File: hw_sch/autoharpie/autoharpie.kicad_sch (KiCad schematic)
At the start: 0 parts

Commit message: DAC, touch sensors
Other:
- added sheet Audio Interface (audio.kicad_sch)
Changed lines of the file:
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@@
+    )
+  )
+  (sheet (at 208.28 72.39) (size 62.23 34.29) (fields_autoplaced)
+    (stroke (width 0.1524) (type solid))
+    (fill (color 0 0 0 0.0000))
+    (property "Sheetname" "Audio Interface" (at 208.28 71.6784 0)
+      (effects (font (size 1.27 1.27)) (justify left bottom))
+    )
+    (property "Sheetfile" "audio.kicad_sch" (at 208.28 107.2646 0)
+      (effects (font (size 1.27 1.27)) (justify left top))
+    )
+    (instances
+      (project "autoharpie"
+        (path "/f22a88c4-866b-40a0-9fc2-96344be0ec71" (page "30"))
+      )
     )
   )

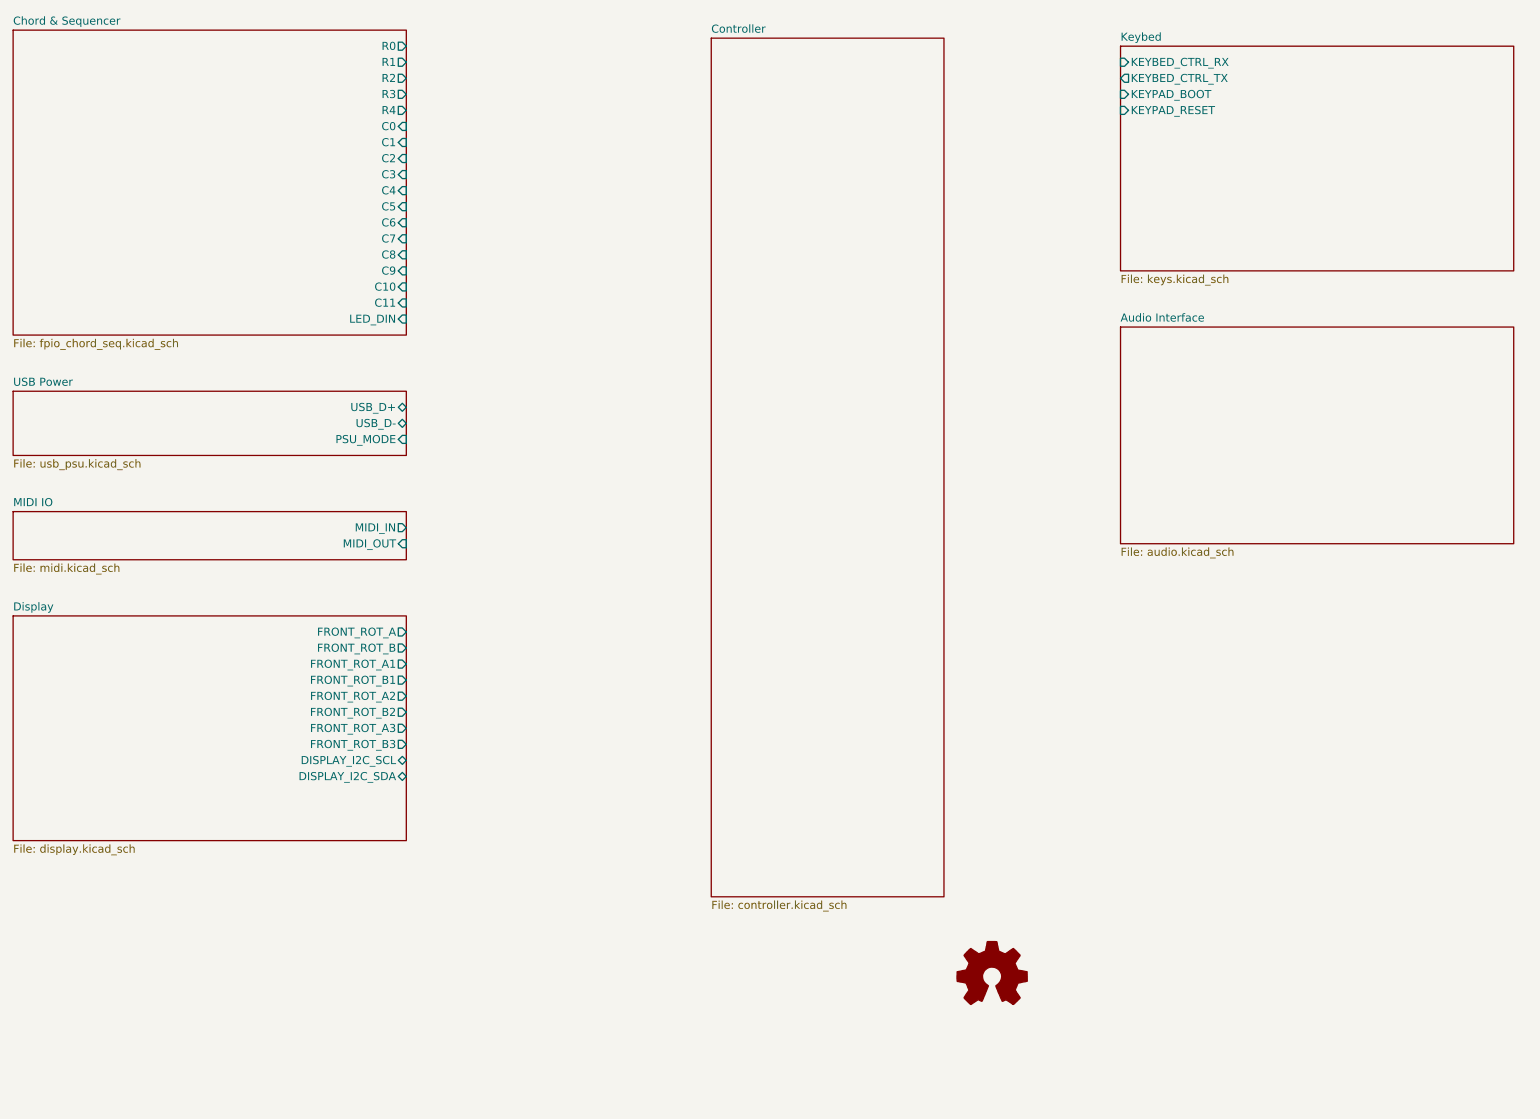
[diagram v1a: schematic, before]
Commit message: DAC wiring, add heirch pins
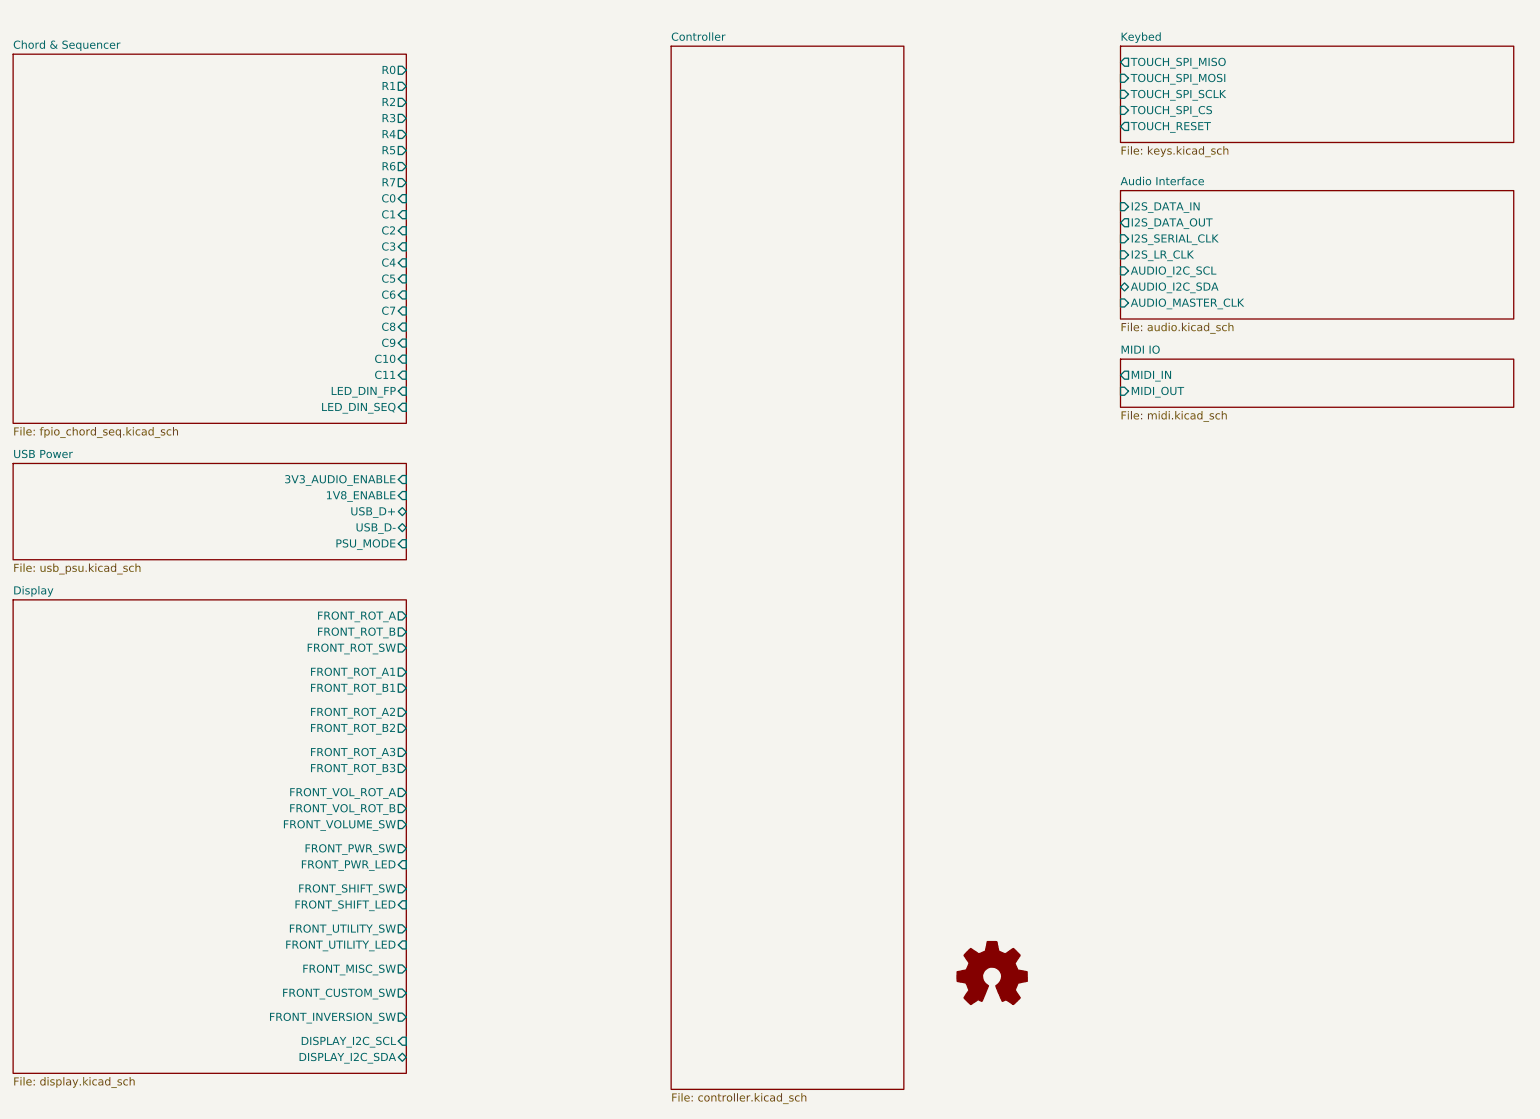
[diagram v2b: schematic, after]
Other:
- sheet Audio Interface ports: added AUDIO_I2C_SCL, AUDIO_I2C_SDA, AUDIO_MASTER_CLK, I2S_DATA_IN, I2S_DATA_OUT, I2S_LR_CLK, I2S_SERIAL_CLK; removed none
- sheet Chord & Sequencer ports: added LED_DIN_FP, LED_DIN_SEQ, R5, R6, R7; removed LED_DIN
- sheet Display ports: added FRONT_CUSTOM_SW, FRONT_INVERSION_SW, FRONT_MISC_SW, FRONT_PWR_LED, FRONT_PWR_SW, FRONT_ROT_SW, FRONT_SHIFT_LED, FRONT_SHIFT_SW, FRONT_UTILITY_LED, FRONT_UTILITY_SW, FRONT_VOLUME_SW, FRONT_VOL_ROT_A, FRONT_VOL_ROT_B; removed none
- sheet Keybed ports: added TOUCH_RESET, TOUCH_SPI_CS, TOUCH_SPI_MISO, TOUCH_SPI_MOSI, TOUCH_SPI_SCLK; removed KEYBED_CTRL_RX, KEYBED_CTRL_TX, KEYPAD_BOOT, KEYPAD_RESET
- sheet USB Power ports: added 1V8_ENABLE, 3V3_AUDIO_ENABLE; removed none

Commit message: keypad
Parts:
- added H1, H2, H3, H4: M2, MountingHole:MountingHole_2.2mm_M2, symbol Mechanical:MountingHole_Pad
- added R1, R23: 10k, Resistor_THT:R_Axial_DIN0204_L3.6mm_D1.6mm_P7.62mm_Horizontal, symbol Device:R
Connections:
- new net +BATT: R1.1
- new net Controller/BATT_ADC: R1.2, R23.2
- new net GND: H1.1, H2.1, H3.1, H4.1, R23.1
- no-connect marks 0 -> 1
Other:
- sheet Chord & Sequencer ports: added none; removed R6, R7
- sheet Controller ports: added BATT_ADC, C0, C1, C10, C11, C2, C3, C4, C5, C6, C7, C8, C9, FRONT_ROT_A, FRONT_ROT_B, FRONT_ROT_SW, I2C_SCL, I2C_SDA, I2S_CK, I2S_MCK, I2S_SD, I2S_WS, LED_DOUT1, LED_DOUT2, MIDI_RX, MIDI_TX, OTG_FS_D+, OTG_FS_D-, OTG_FS_ID, PSU_MODE, PWR_LED, PWR_SW, R0, R1, R2, R3, R4, R5, SPI_MISO, SPI_MOSI, SPI_NSS, SPI_SCK, TOUCH_RESET; removed none
- sheet Display ports: added none; removed FRONT_CUSTOM_SW, FRONT_INVERSION_SW, FRONT_MISC_SW, FRONT_ROT_A1, FRONT_ROT_A2, FRONT_ROT_A3, FRONT_ROT_B1, FRONT_ROT_B2, FRONT_ROT_B3, FRONT_SHIFT_LED, FRONT_SHIFT_SW, FRONT_UTILITY_LED, FRONT_UTILITY_SW, FRONT_VOLUME_SW, FRONT_VOL_ROT_A, FRONT_VOL_ROT_B
- sheet USB Power ports: added none; removed 1V8_ENABLE, 3V3_AUDIO_ENABLE

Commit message: rev 0.1 pcb
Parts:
- removed R1, R23: 10k, Resistor_THT:R_Axial_DIN0204_L3.6mm_D1.6mm_P7.62mm_Horizontal, symbol Device:R
- added H3, H4, H7, H8: M2, MountingHole:MountingHole_2.2mm_M2, symbol Mechanical:MountingHole_Pad
- renumbered H3 to H5, H4 to H6
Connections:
- net GND: now also H3.1, H4.1, H7.1, H8.1
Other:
- sheet Chord & Sequencer ports: added LED_DIN; removed LED_DIN_FP, LED_DIN_SEQ, R5
- sheet Controller ports: added I2C1_SCL, I2C1_SDA, I2C3_SCL, I2C3_SDA, LED_DOUT, TOUCH_WAKE; removed BATT_ADC, I2C_SCL, I2C_SDA, LED_DOUT1, LED_DOUT2, OTG_FS_D+, OTG_FS_D-, OTG_FS_ID, PSU_MODE, PWR_LED, PWR_SW, R5, SPI_MISO, SPI_MOSI, SPI_NSS, SPI_SCK
- sheet Display ports: added none; removed FRONT_PWR_LED, FRONT_PWR_SW
- sheet Keybed ports: added RESET, TOUCH_SCL, TOUCH_SDA, WAKE; removed TOUCH_RESET, TOUCH_SPI_CS, TOUCH_SPI_MISO, TOUCH_SPI_MOSI, TOUCH_SPI_SCLK
- sheet USB Power ports: added none; removed PSU_MODE, USB_D+, USB_D-
- moved on the sheet: H1, H2, H5, H6

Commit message: ic fix atept
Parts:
- added H9: M2, MountingHole:MountingHole_2.2mm_M2_DIN965_Pad, symbol Mechanical:MountingHole_Pad
- H1, H2, H3, H4, H5, H6, H7, H8: footprint MountingHole:MountingHole_2.2mm_M2 -> MountingHole:MountingHole_2.2mm_M2_DIN965_Pad
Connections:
- net GND: now also H9.1
- no-connect marks 1 -> 0
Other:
- sheet Audio Interface ports: added none; removed I2S_DATA_OUT

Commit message: new icc
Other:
- sheet Audio Interface ports: added INT; removed none
- sheet Controller ports: added AUDIO_IRQ; removed none
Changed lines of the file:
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@@
+    (stroke (width 0) (type default))
+  )
+  (wire (pts (xy 173.99 55.88) (xy 208.28 55.88))
     (stroke (width 0) (type default))
   )
@@
   (symbol (lib_id "power:GND") (at 191.77 151.13 0) (unit 1)
     (in_bom yes) (on_board yes) (dnp no) (fields_autoplaced)
-    (property "Reference" "#PWR0145" (at 191.77 157.48 0)
+    (property "Reference" "#PWR09" (at 191.77 157.48 0)
       (effects (font (size 1.27 1.27)) hide)
     )
@@
       (project "autoharpie"
         (path "/f22a88c4-866b-40a0-9fc2-96344be0ec71"
-          (reference "#PWR0145") (unit 1)
+          (reference "#PWR09") (unit 1)
         )
       )
@@
       (effects (font (size 1.27 1.27)) (justify left))
     )
+    (pin "AUDIO_IRQ" input (at 173.99 55.88 0)
+      (effects (font (size 1.27 1.27)) (justify right))
+    )
     (instances
       (project "autoharpie"
@@
       (effects (font (size 1.27 1.27)) (justify left))
     )
+    (pin "INT" output (at 208.28 55.88 180)
+      (effects (font (size 1.27 1.27)) (justify left))
+    )

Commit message: final final final 0.1 rev
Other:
- sheet Controller ports: added none; removed I2C3_SCL, I2C3_SDA
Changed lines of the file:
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@@
+    (stroke (width 0) (type default))
+  )
+  (wire (pts (xy 95.25 121.92) (xy 100.33 121.92))
     (stroke (width 0) (type default))
   )
@@
     (stroke (width 0) (type default))
   )
+  (wire (pts (xy 95.25 119.38) (xy 100.33 119.38))
+    (stroke (width 0) (type default))
+  )
   (wire (pts (xy 200.66 63.5) (xy 208.28 63.5))
     (stroke (width 0) (type default))
   )
+  (wire (pts (xy 200.66 31.75) (xy 208.28 31.75))
+    (stroke (width 0) (type default))
+  )
   (wire (pts (xy 173.99 58.42) (xy 208.28 58.42))
     (stroke (width 0) (type default))
   )
-  (wire (pts (xy 129.54 119.38) (xy 137.16 119.38))
+  (wire (pts (xy 132.08 119.38) (xy 137.16 119.38))
     (stroke (width 0) (type default))
   )
@@
     (stroke (width 0) (type default))
   )
-  (wire (pts (xy 102.87 119.38) (xy 95.25 119.38))
-    (stroke (width 0) (type default))
-  )
   (wire (pts (xy 95.25 129.54) (xy 137.16 129.54))
     (stroke (width 0) (type default))
@@
     (stroke (width 0) (type default))
   )
-  (wire (pts (xy 129.54 121.92) (xy 137.16 121.92))
-    (stroke (width 0) (type default))
-  )
-  (wire (pts (xy 102.87 121.92) (xy 95.25 121.92))
+  (wire (pts (xy 200.66 34.29) (xy 208.28 34.29))
+    (stroke (width 0) (type default))
+  )
+  (wire (pts (xy 132.08 121.92) (xy 137.16 121.92))
     (stroke (width 0) (type default))
   )
@@
     (stroke (width 0) (type default))
   )
-  (wire (pts (xy 173.99 34.29) (xy 208.28 34.29))
-    (stroke (width 0) (type default))
-  )
-  (wire (pts (xy 173.99 31.75) (xy 208.28 31.75))
-    (stroke (width 0) (type default))
-  )
   (wire (pts (xy 95.25 62.23) (xy 137.16 62.23))
     (stroke (width 0) (type default))
   )
-  (label "I2C_SDA" (at 129.54 121.92 180) (fields_autoplaced)
+  (label "I2C_SCL" (at 100.33 121.92 0) (fields_autoplaced)
+    (effects (font (size 1.27 1.27)) (justify left bottom))
+  )
+  (label "I2C_SCL" (at 200.66 31.75 180) (fields_autoplaced)
     (effects (font (size 1.27 1.27)) (justify right bottom))
   )
-  (label "I2C_SDA" (at 102.87 121.92 0) (fields_autoplaced)
+  (label "I2C_SDA" (at 100.33 119.38 0) (fields_autoplaced)
     (effects (font (size 1.27 1.27)) (justify left bottom))
   )
-  (label "I2C_SCL" (at 102.87 119.38 0) (fields_autoplaced)
-    (effects (font (size 1.27 1.27)) (justify left bottom))
+  (label "I2C_SDA" (at 132.08 119.38 180) (fields_autoplaced)
+    (effects (font (size 1.27 1.27)) (justify right bottom))
+  )
+  (label "I2C_SCL" (at 132.08 121.92 180) (fields_autoplaced)
+    (effects (font (size 1.27 1.27)) (justify right bottom))
   )
   (label "I2C_SDA" (at 200.66 66.04 180) (fields_autoplaced)
     (effects (font (size 1.27 1.27)) (justify right bottom))
   )
-  (label "I2C_SCL" (at 129.54 119.38 180) (fields_autoplaced)
+  (label "I2C_SDA" (at 200.66 34.29 180) (fields_autoplaced)
     (effects (font (size 1.27 1.27)) (justify right bottom))
   )
@@
       (effects (font (size 1.27 1.27)) (justify left))
     )
-    (pin "I2C1_SDA" bidirectional (at 173.99 31.75 0)
-      (effects (font (size 1.27 1.27)) (justify right))
-    )
-    (pin "I2C1_SCL" output (at 173.99 34.29 0)
-      (effects (font (size 1.27 1.27)) (justify right))
-    )
     (pin "C7" output (at 137.16 69.85 180)
       (effects (font (size 1.27 1.27)) (justify left))
@@
       (effects (font (size 1.27 1.27)) (justify left))
     )
-    (pin "I2C3_SCL" output (at 137.16 121.92 180)
-      (effects (font (size 1.27 1.27)) (justify left))
-    )
-    (pin "I2C3_SDA" bidirectional (at 137.16 119.38 180)
-      (effects (font (size 1.27 1.27)) (justify left))
-    )
     (pin "AUDIO_IRQ" input (at 173.99 55.88 0)
       (effects (font (size 1.27 1.27)) (justify right))
     )
-    (instances
+    (pin "I2C1_SCL" output (at 137.16 121.92 180)
+      (effects (font (size 1.27 1.27)) (justify left))
+    )
+    (pin "I2C1_SDA" bidirectional (at 137.16 119.38 180)
+      (effects (font (size 1.27 1.27)) (justify left))
+    )
+    (instances
